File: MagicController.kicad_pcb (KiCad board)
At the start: 2 copper layers, 100 x 100 mm, 28 parts, among them SW1 TS-1187A-B-A-B, SW2 TS-1187A-B-A-B, U1 CH340C_C7464026, U2 AMS1117-3.3, U3 ESP32-WROOM-32E(8MB), U4 ESP32-S3-WROOM-1, U5 DS18B20U, U6 CH224K

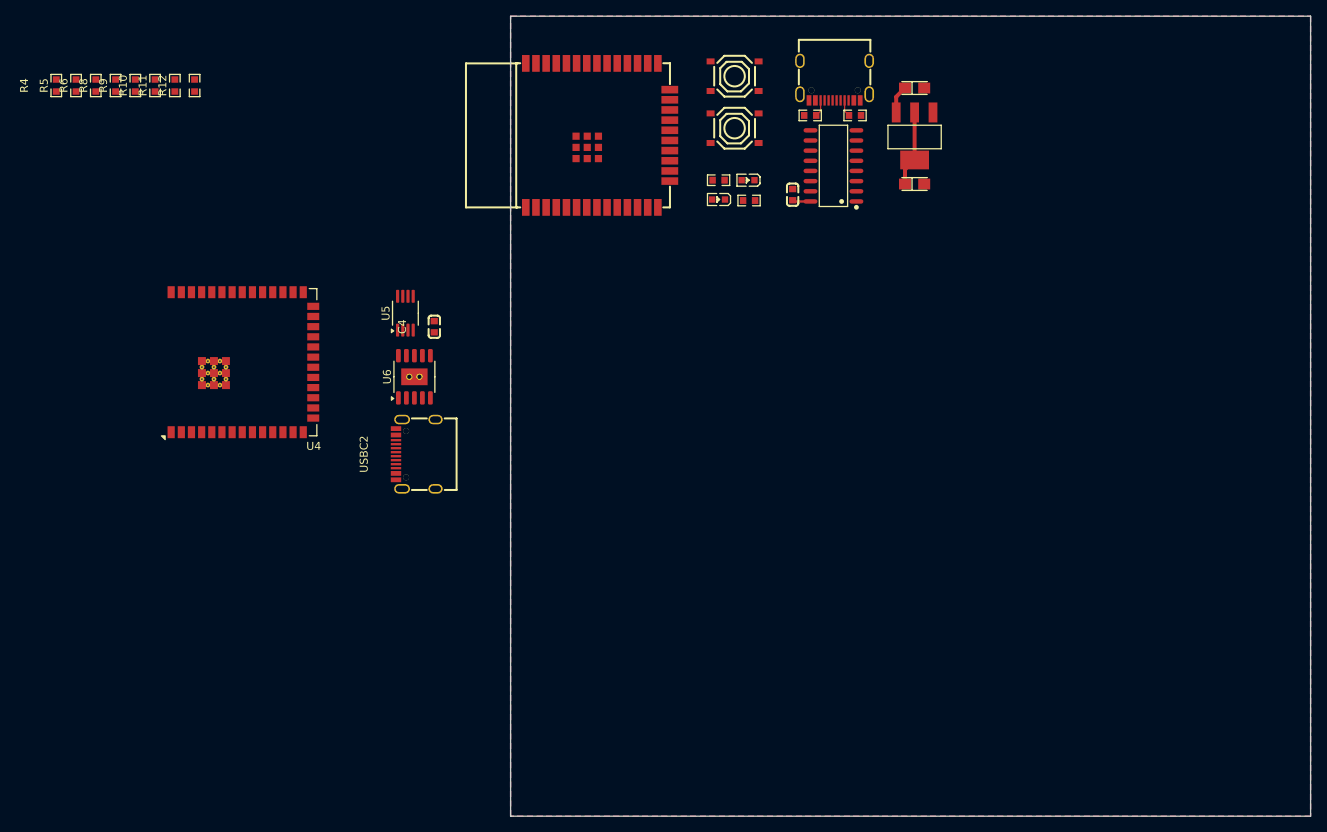
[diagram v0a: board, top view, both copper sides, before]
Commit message: easyeda2kidad from csv
añadido script para cargar las libs
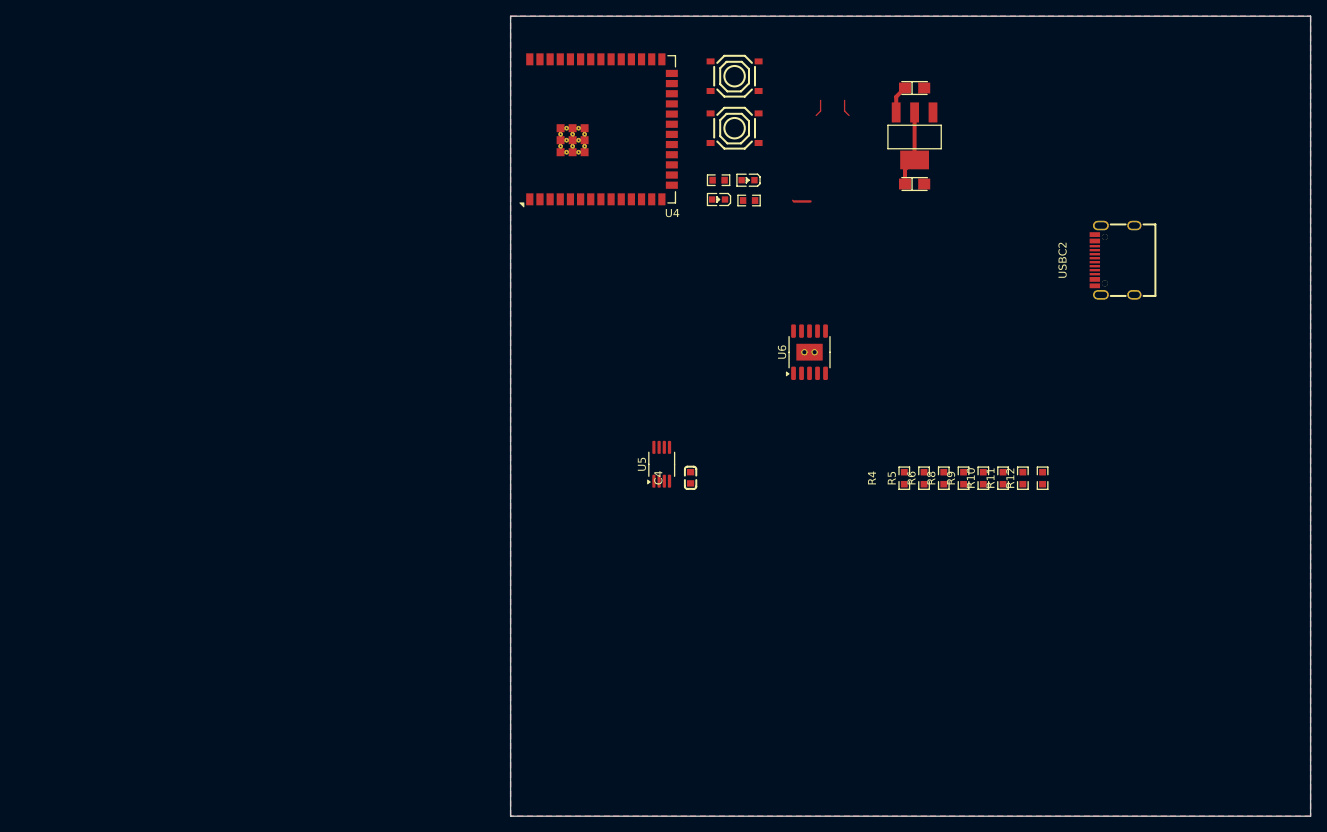
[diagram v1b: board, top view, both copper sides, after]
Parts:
- removed C1: 0.1u, easyeda2kicad:C0603
- removed R1, R2: 5k1, easyeda2kicad:R0603
- removed U1: CH340C_C7464026, easyeda2kicad:SOP-16_L10.0-W3.9-P1.27-LS6.0-BL
- removed U3: ESP32-WROOM-32E(8MB), easyeda2kicad:WIFI-SMD_ESP32-WROOM-32E
- removed USBC1: TYPE-C-31-M-12, easyeda2kicad:USB-C_SMD-TYPE-C-31-M-12
- moved R10 116.8 mm to (143.3, 106.4)
- moved R11 116.8 mm to (145.8, 106.4)
- moved R12 116.8 mm to (148.3, 106.4)
- moved R4 116.8 mm to (131.0, 106.4)
- moved R5 116.8 mm to (133.5, 106.4)
- moved R6 116.8 mm to (135.9, 106.4)
- moved R8 116.8 mm to (138.4, 106.4)
- moved R9 116.8 mm to (140.9, 106.4)
- moved USBC2 90.7 mm to (157.3, 79.1)
- moved U4 53.5 mm to (89.4, 62.8)
- moved U6 49.5 mm to (119.2, 90.6)
- moved C4 37.2 mm to (104.3, 106.3)
- moved U5 37.2 mm to (100.7, 104.7)
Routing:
- net (no net): track 0.00 -> 4.23 mm
- net Net-(USBC1-CC1): track 2.11 -> 0.00 mm
- net Net-(USBC1-CC2): track 2.11 -> 0.00 mm
